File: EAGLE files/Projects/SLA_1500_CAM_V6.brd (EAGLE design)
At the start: 37.8 x 26.4 mm, 87 parts, among them J2 JST GH SM06B, J3 MOLEX 53261-03, J4 MOLEX 53261-04, J5 MOLEX 53261-04, J6 MOLEX 53261-04, U10 TPS73633DBVR, U11 TXS0102, U8 TXS0102, U9 TXS0102

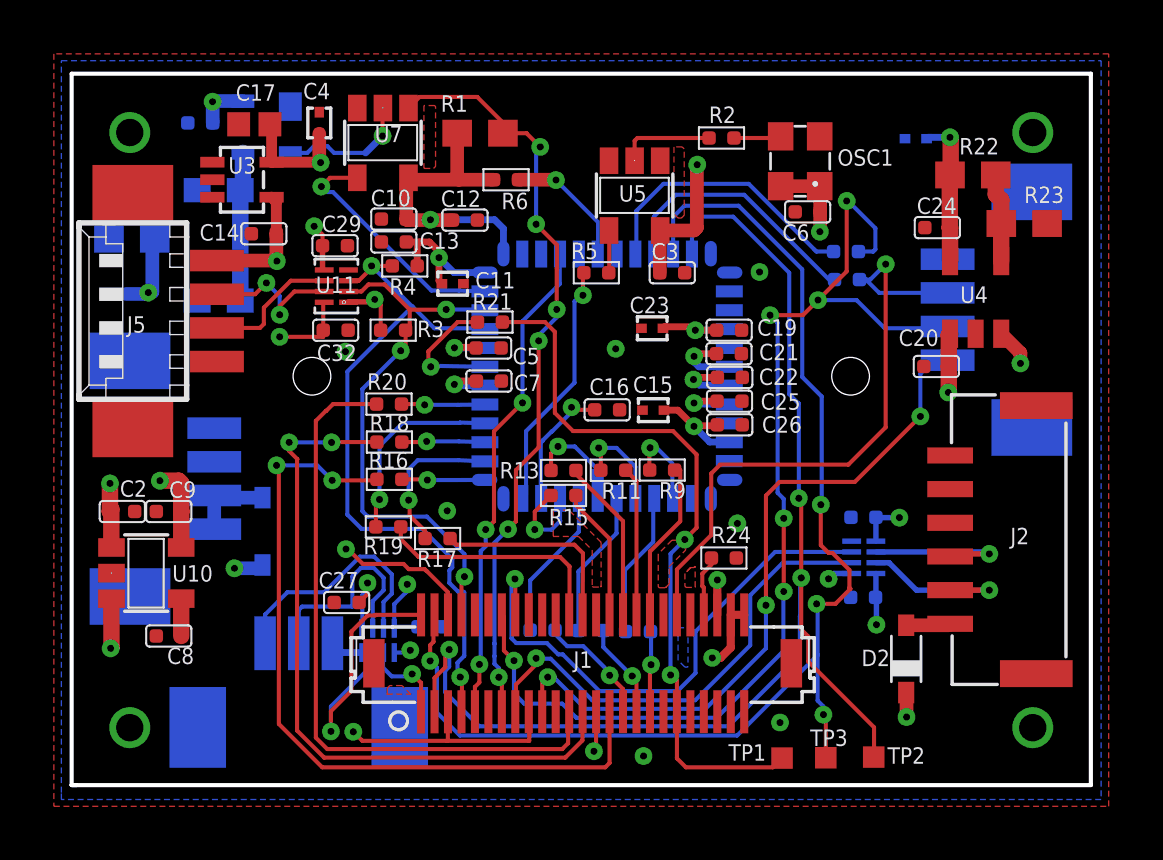
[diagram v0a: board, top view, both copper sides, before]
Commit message: Update SLA1500 CAM V6
Repositioned C16 and C18 coupling capacitors
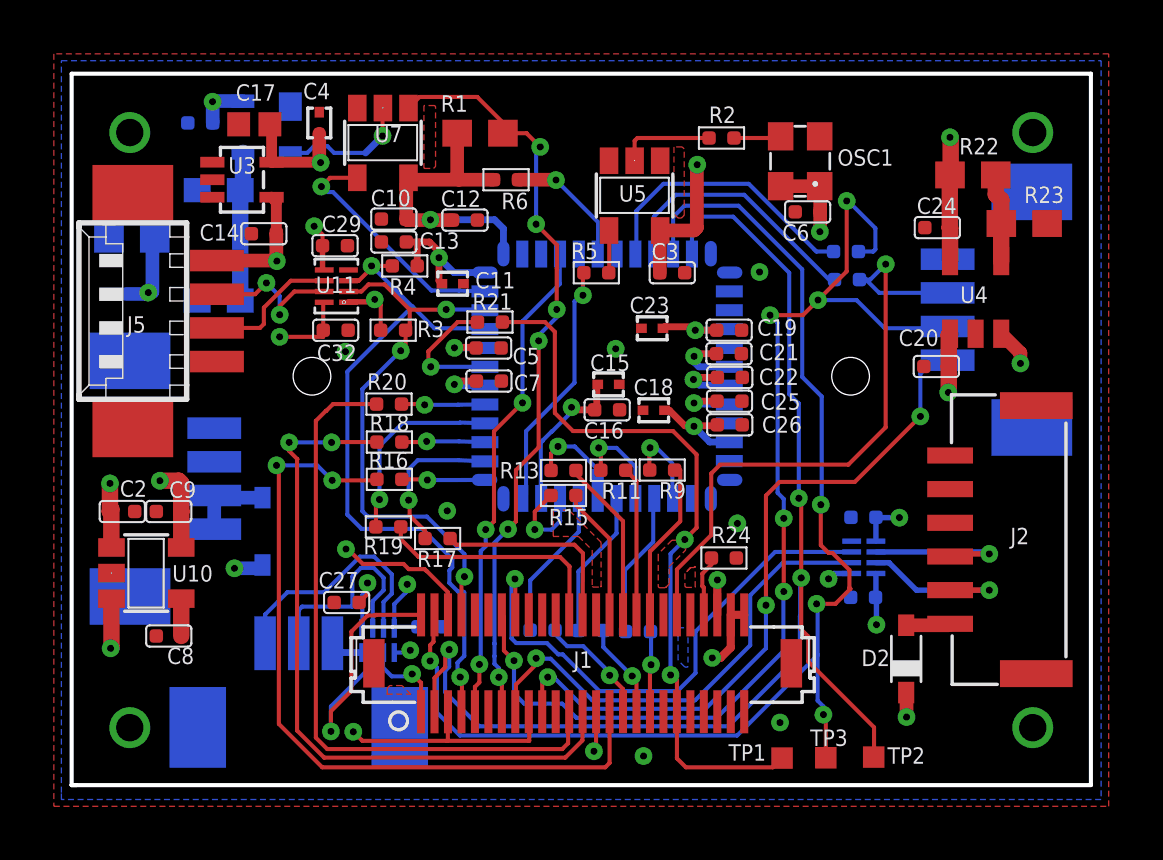
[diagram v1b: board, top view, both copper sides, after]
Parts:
- moved C18 14.0 mm to (2.69, -1.30), flipped to the top, turned to 180 degrees
- moved C15 1.92 mm to (1.01, -0.33), turned to 0 degrees
